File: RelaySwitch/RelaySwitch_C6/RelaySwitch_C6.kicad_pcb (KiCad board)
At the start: 2 copper layers, 67.5 x 52 mm, 39 parts, among them J1 AC_MAINS_IN, J3 LOAD_CH1, J4 LOAD_CH2, J5 SW1_INPUT, J6 SW2_INPUT, K1 G5Q-1-DC5, K2 G5Q-1-DC5, Q1 MMBT8050, Q2 MMBT8050, U1 HLK-2M05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

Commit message: 07/03
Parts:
- removed R10: 1m, Resistor_SMD:R_2512_6332Metric
- added C2: 10u, Capacitor_SMD:C_0402_1005Metric, B.Cu at (190.5, 80.0)
- added C3: 100n, Capacitor_SMD:C_0402_1005Metric, B.Cu at (186.5, 79.5)
- R18: footprint Resistor_SMD:R_Shunt_Vishay_WSK2512_6332Metric_T2.66mm -> XIAO_Series_Footprints:RES_WSK2512R0100FEA
- U2: footprint XIAO_Series_Footprints:XIAO-ESP32-S3-DIP -> XIAO_Series_Footprints:XIAO-ESP32-C6-DIP
- moved C5 31.1 mm to (192.5, 80.0), turned to 0 degrees
- moved R18 12.0 mm to (146.5, 66.5), turned to -90 degrees
- moved C1 0.71 mm to (168.5, 97.5)
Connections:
- C5 pad 1: +3V3 -> +5V
- U5 pad 3: GND -> Net-(U5-V1N)
- U5 pad 4: /L -> GND
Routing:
- net Net-(U5-V1N): track 0.00 -> 32.1 mm, vias 0 -> 1
- net /L: track 57.7 -> 41.3 mm, vias 2 -> 1
- net /L_Sense: track 26.0 -> 35.2 mm
- net GND: track 146.9 -> 139.4 mm, vias 26 -> 19
- net Net-(J5-Pin_1): track 97.5 -> 91.2 mm
- net Net-(D1-A): track 85.4 -> 81.0 mm
- net /RELAY_CH1_IN: track 58.2 -> 55.1 mm
- net /RELAY_CH2_IN: track 53.6 -> 51.2 mm
- net Net-(U5-V1P): track 43.6 -> 45.9 mm
- net +5V: track 123.4 -> 125.4 mm
- net +3V3: track 35.6 -> 37.2 mm
- net /LOAD_CH1: track 29.0 -> 30.3 mm
- net Net-(J6-Pin_1): track 41.7 -> 40.6 mm
- net /LOAD_CH2: track 15.0 -> 14.2 mm

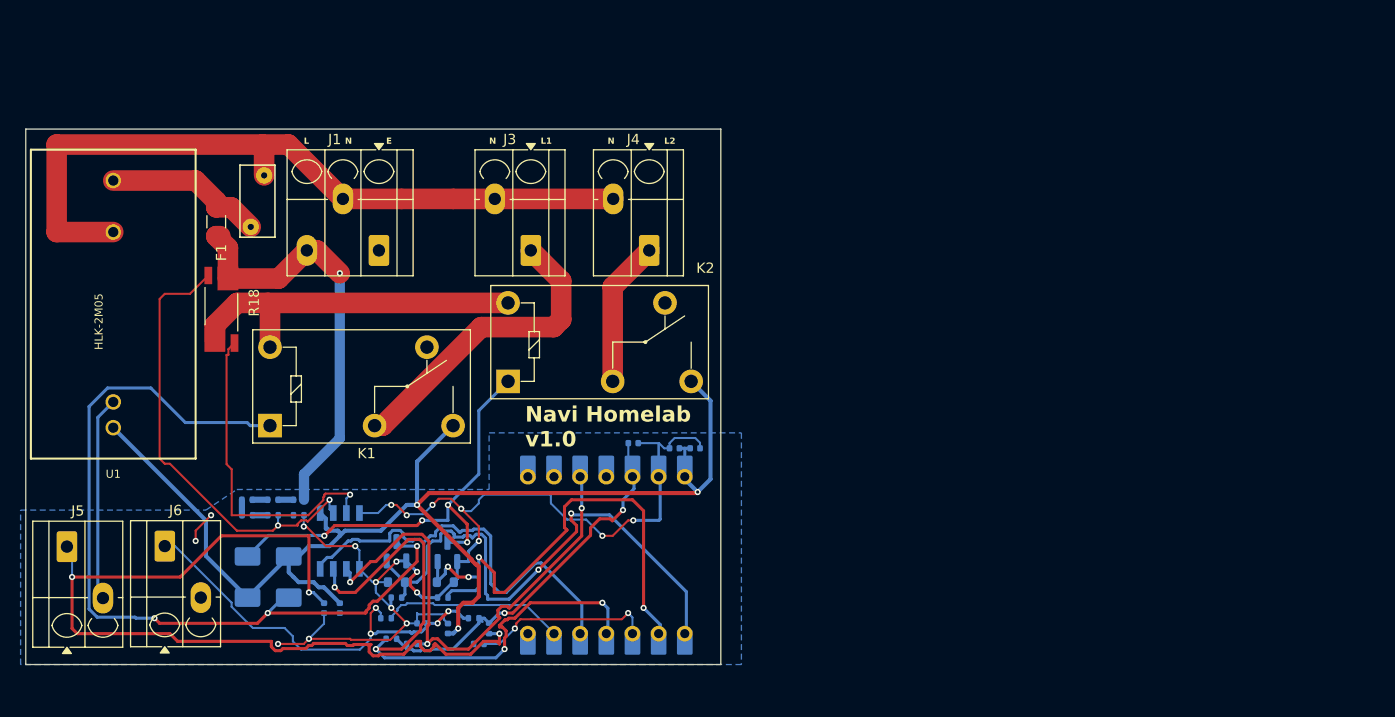
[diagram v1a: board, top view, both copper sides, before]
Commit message: Reduced relay size
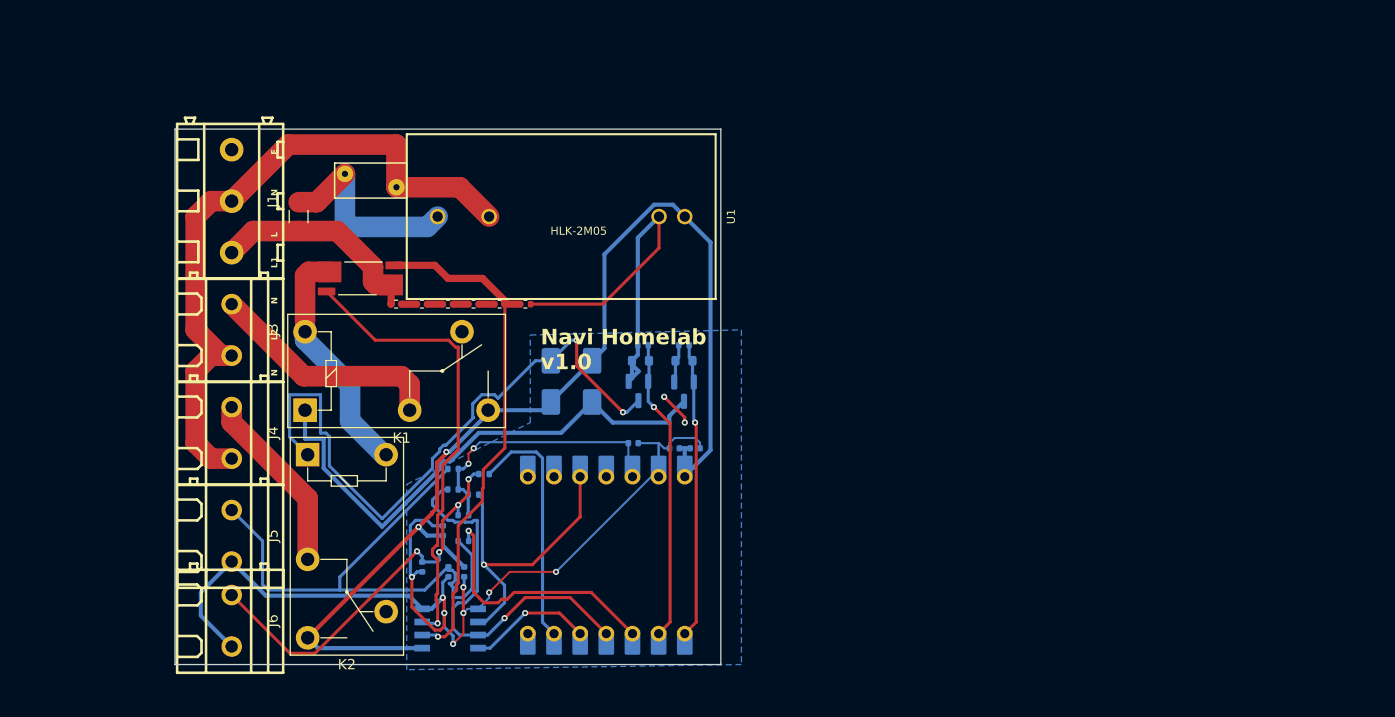
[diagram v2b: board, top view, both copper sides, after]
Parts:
- J1: footprint TerminalBlock_Degson:TerminalBlock_Degson_DG250-3.5-03P_1x03_P3.50mm_45Degree -> seeed esp32:CONN-TH_3P-P5.00_WJ128V-5.0-3P
- J3, J4, J5, J6: footprint TerminalBlock_Degson:TerminalBlock_Degson_DG250-3.5-02P_1x02_P3.50mm_45Degree -> seeed esp32:CONN-TH_2P-P5.00_WJ128V-5.0-2P
- R13, R4, R6, R7, R8, R9: moved to F.Cu
- U5: footprint XIAO_Series_Footprints:SOIC8 -> seeed esp32:SOIC8
- moved U1 44.3 mm to (179.5, 57.5), turned to 0 degrees
- moved J4 44.3 mm to (147.5, 78.5), turned to -90 degrees
- moved D1 37.8 mm to (182.5, 73.5), turned to -90 degrees
- moved R2 37.1 mm to (191.4, 70.0)
- moved R1 35.2 mm to (191.4, 71.5)
- moved D2 32.3 mm to (178.5, 73.5), turned to 90 degrees
- moved Q1 31.9 mm to (191.4, 74.5), turned to -90 degrees
- moved R5 31.3 mm to (187.4, 70.0)
- moved R13 30.1 mm to (173.5, 66.0)
- moved R9 30.1 mm to (176.0, 66.0)
- moved J3 30.1 mm to (147.5, 68.5), turned to -90 degrees
- moved R8 30.0 mm to (171.0, 66.0)
- moved R3 28.7 mm to (187.2, 71.5), turned to 180 degrees
- moved R7 27.2 mm to (168.5, 66.0), turned to 0 degrees
- moved Q2 24.3 mm to (187.0, 74.4), turned to -90 degrees
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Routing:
- net Net-(C7-Pad1): track 91.2 -> 55.3 mm, vias 3 -> 0
- net Net-(D1-A): track 81.0 -> 52.0 mm, vias 3 -> 0
- net /HLW_SEL: track 40.9 -> 12.2 mm, vias 0 -> 1
- net /RELAY_CH1_IN: track 55.1 -> 28.7 mm, vias 2 -> 1
- net /RELAY_CH2_IN: track 51.2 -> 29.4 mm, vias 4 -> 1
- net /HLW_CF1: track 58.5 -> 37.6 mm, vias 4 -> 1
- net /L: track 41.3 -> 21.2 mm, vias 1 -> 0
- net /HLW_CF: track 49.7 -> 30.1 mm, vias 3 -> 1
- net Net-(D2-A): track 43.7 -> 63.1 mm, vias 4 -> 2
- net +5V: track 125.4 -> 110.8 mm, vias 3 -> 2
- net /L_Sense: track 35.2 -> 22.3 mm
- net Net-(U5-V1N): track 32.1 -> 44.9 mm
- net +3V3: track 37.2 -> 26.0 mm
- net Net-(U2-GPIO2_A2_D2): track 17.6 -> 25.1 mm, vias 2 -> 1
- net GND: track 139.4 -> 146.7 mm, vias 19 -> 10
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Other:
- board size 67.5 x 52 mm -> 53 x 52 mm

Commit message: For review
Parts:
- C2: footprint Capacitor_SMD:C_0402_1005Metric -> Capacitor_SMD:C_0805_2012Metric
- F1: value ~ -> T250mA/250V
- moved C2 1.41 mm to (189.5, 79.0)
- moved C3 0.50 mm to (186.0, 79.5)
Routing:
- net GND: track 146.7 -> 150.6 mm
- net +5V: track 110.8 -> 113.9 mm
- net Net-(D1-A): track 52.0 -> 51.5 mm
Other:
- outline, holes or cut-outs redrawn

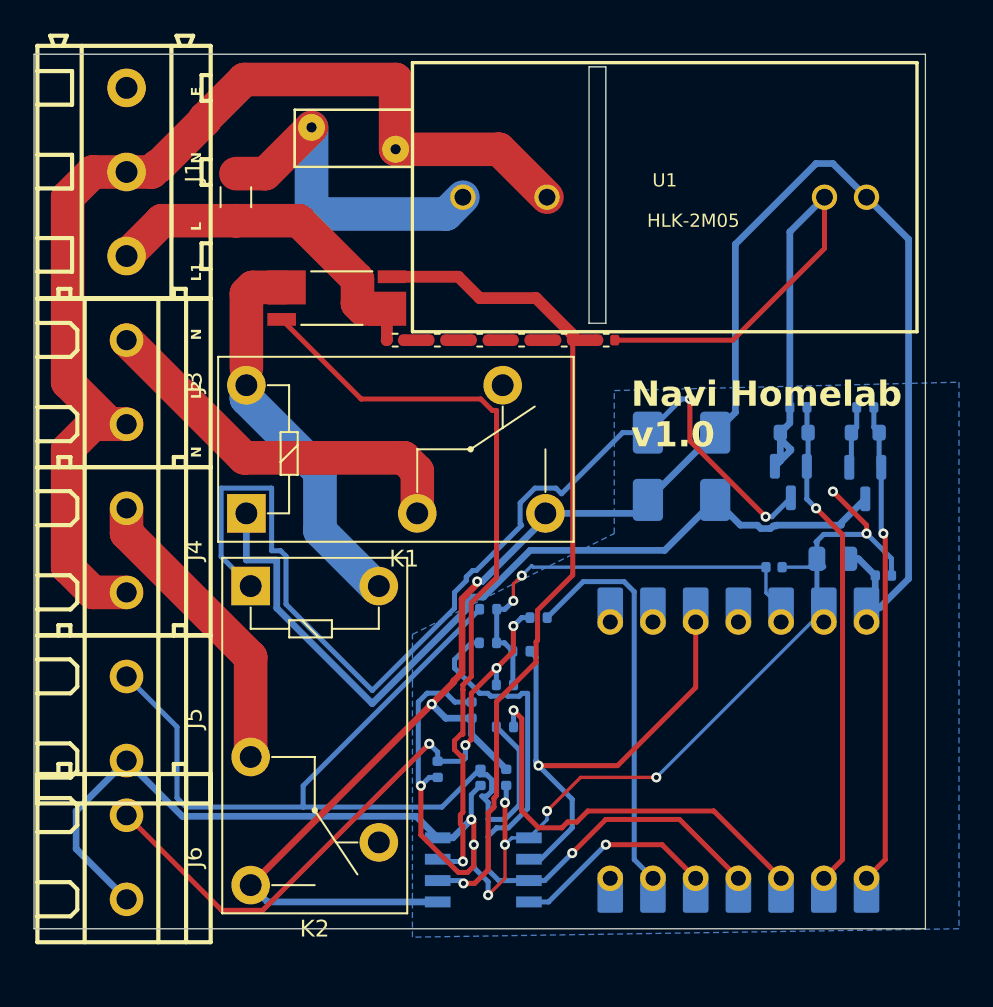
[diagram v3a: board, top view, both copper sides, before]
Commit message: warning fix - 17 left
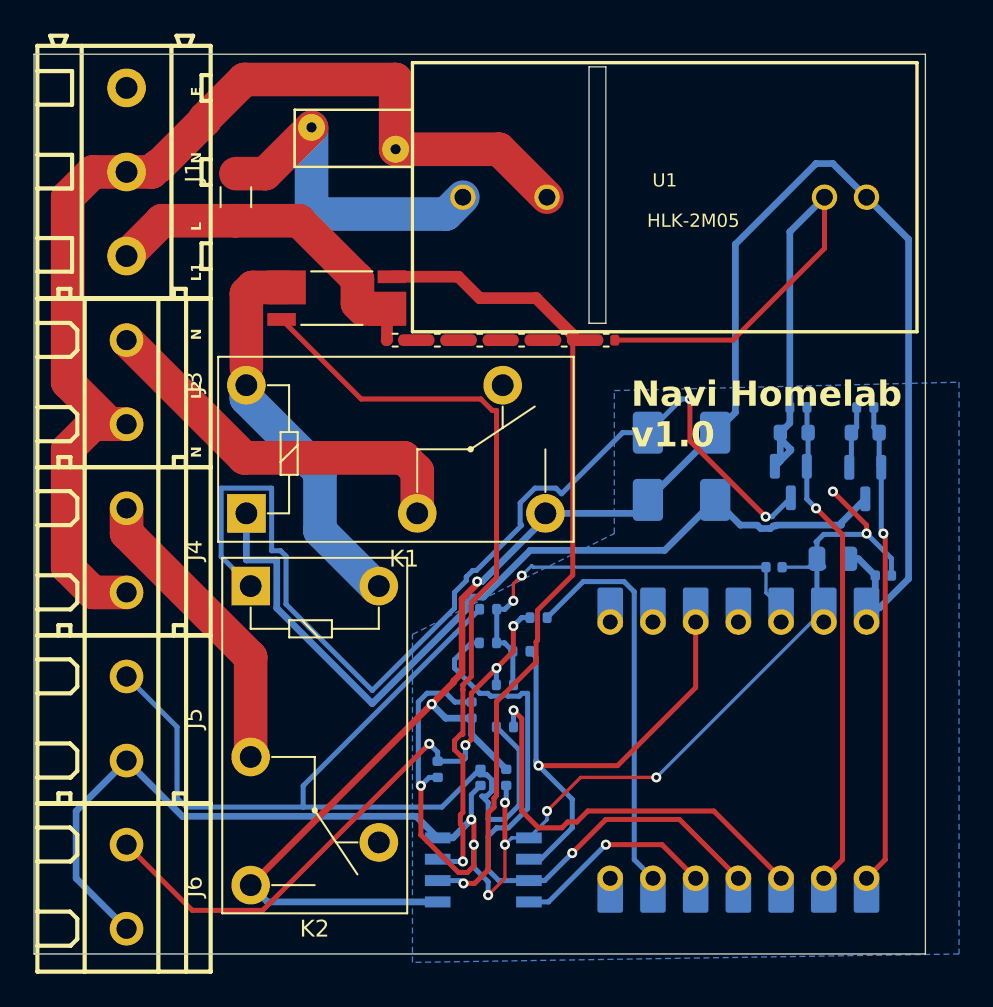
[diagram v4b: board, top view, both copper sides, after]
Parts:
- moved J6 1.75 mm to (147.5, 98.5)
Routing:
- net GND: track 150.6 -> 152.3 mm
- net Net-(C8-Pad1): track 38.7 -> 37.9 mm
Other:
- board size 53 x 52 mm -> 53 x 53.5 mm
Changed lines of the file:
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@@
 			(crossoutdnponfab yes)
 			(subtractmaskfromsilk no)
-			(outputformat 1)
+			(outputformat 5)
 			(mirror no)
-			(drillshape 1)
+			(drillshape 0)
 			(scaleselection 1)
-			(outputdirectory "")
+			(outputdirectory "../Review/")
 		)
 	)
@@
 	(footprint "seeed esp32:CONN-TH_2P-P5.00_WJ128V-5.0-2P"
 		(layer "F.Cu")
-		(at 147.5 96.75 -90)
+		(at 147.5 98.5 -90)
 		(property "Reference" "J6"
 			(at 0 -4 90)
@@
 	)
 	(gr_line
-		(start 142 101)
+		(start 142 102.5)
 		(end 142 49)
 		(stroke
@@
 	(gr_line
 		(start 195 49)
-		(end 195 101)
+		(end 195 102.5)
 		(stroke
 			(width 0.05)
@@
 	)
 	(gr_line
-		(start 195 101)
-		(end 142 101)
+		(start 195 102.5)
+		(end 142 102.5)
 		(stroke
 			(width 0.05)
@@
 	)
 	(segment
-		(start 144.5 94)
-		(end 147.5 91)
+		(start 147.5 91)
+		(end 144.5 94)
 		(width 0.4)
 		(layer "B.Cu")
@@
 	)
 	(segment
-		(start 147.5 99.25)
-		(end 144.5 96.25)
-		(width 0.4)
+		(start 190.915 70)
+		(end 190.915 71.185)
+		(width 0.3)
 		(layer "B.Cu")
 		(net 3)
 	)
 	(segment
-		(start 190.915 70)
-		(end 190.915 71.185)
-		(width 0.3)
+		(start 144.5 98)
+		(end 147.5 101)
+		(width 0.4)
 		(layer "B.Cu")
 		(net 3)
@@
 	)
 	(segment
+		(start 144.5 94)
+		(end 144.5 98)
+		(width 0.4)
+		(layer "B.Cu")
+		(net 3)
+	)
+	(segment
 		(start 186.94 70)
 		(end 186.94 70.935)
@@
 	)
 	(segment
-		(start 144.5 96.25)
-		(end 144.5 94)
-		(width 0.4)
-		(layer "B.Cu")
-		(net 3)
-	)
-	(segment
 		(start 171.424 95.595)
 		(end 170.405 95.595)
@@
 	)
 	(segment
-		(start 153.156 99.906)
-		(end 155.594 99.906)
+		(start 155.594 99.906)
+		(end 151.406 99.906)
 		(width 0.3)
 		(layer "F.Cu")
@@
 	)
 	(segment
-		(start 147.5 94.25)
-		(end 153.156 99.906)
+		(start 151.406 99.906)
+		(end 147.5 96)
 		(width 0.3)
 		(layer "F.Cu")
@@
 	)
 	(segment
-		(start 155.594 99.906)
-		(end 165.5 90)
+		(start 168 89.734948)
+		(end 168 87)
 		(width 0.3)
 		(layer "F.Cu")
@@
 	)
 	(segment
-		(start 168 89.734948)
-		(end 168 87)
+		(start 167.649999 90.084949)
+		(end 168 89.734948)
 		(width 0.3)
 		(layer "F.Cu")
@@
 	)
 	(segment
-		(start 167.649999 90.084949)
-		(end 168 89.734948)
+		(start 165.5 90)
+		(end 155.594 99.906)
 		(width 0.3)
 		(layer "F.Cu")
@@
 		(polygon
 			(pts
-				(xy 176 65.336264) (xy 176 48.836264) (xy 177.5 48.836264) (xy 177.5 65.336264)
+				(xy 176.5 65.336264) (xy 176.5 48.836264) (xy 178 48.836264) (xy 178 65.336264)
 			)
 		)
@@
 		(polygon
 			(pts
-				(xy 164.5 85.5) (xy 164.5 83.5) (xy 176.5 77.5) (xy 176.5 69) (xy 197 68.5) (xy 197 101) (xy 164.5 101.5)
+				(xy 164.5 85.5) (xy 164.5 83.5) (xy 176.5 77.5) (xy 176.5 69) (xy 197 68.5) (xy 197 102.5) (xy 164.5 103)
 				(xy 164.5 86.5)
 			)

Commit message: Fixed relay connections and F1 Fuse
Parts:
- added C10: 33n, Capacitor_SMD:C_0402_1005Metric, F.Cu at (213.6, 78.9)
- added C11: 33n, Capacitor_SMD:C_0402_1005Metric, F.Cu at (213.6, 80.9)
- added C4: 0.1u, Capacitor_SMD:C_0402_1005Metric, F.Cu at (213.6, 75.0)
- added C9: 33n, Capacitor_SMD:C_0402_1005Metric, F.Cu at (213.6, 77.0)
- added R19: 1k, Resistor_SMD:R_0402_1005Metric, F.Cu at (216.5, 75.0)
- added R20: 1k, Resistor_SMD:R_0402_1005Metric, F.Cu at (216.5, 77.0)
- C6: value 100n -> 10u
- F1: footprint Fuse:Fuse_1206_3216Metric -> Fuse:Fuseholder_Clip-5x20mm_Littelfuse_111_Inline_P20.00x5.00mm_D1.05mm_Horizontal
- moved R18 49.9 mm to (209.5, 57.5)
- moved RV1 24.4 mm to (180.0, 41.9)
- moved F1 14.6 mm to (152.0, 43.0), turned to 0 degrees
- moved K1 9.97 mm to (161.8, 69.4), turned to 90 degrees
- moved R6 1.76 mm to (167.7, 66.0)
- moved R13 1.75 mm to (175.3, 66.0)
- moved R4 1.75 mm to (165.2, 66.0)
- moved R7 1.75 mm to (170.3, 66.0)
- moved R8 1.75 mm to (172.7, 66.0)
- moved R9 1.75 mm to (177.8, 66.0)
- moved K2 1.65 mm to (154.2, 82.1)
- moved J1 0.91 mm to (146.6, 56.0)
- moved J3 0.91 mm to (146.6, 68.5)
- moved J4 0.91 mm to (146.6, 78.5)
- moved J5 0.91 mm to (146.6, 88.5)
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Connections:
- F1 pad 2: /MAINS_L -> GND
- K1 pad 1: Net-(D1-A) -> +5V
- K1 pad 3: +5V -> Net-(D1-A)
- K2 pad 1: Net-(D2-A) -> +5V
- K2 pad 3: +5V -> Net-(D2-A)
- Q1 pad 2: /RELAY_CH1_IN -> Net-(Q1-B)
- Q2 pad 2: /RELAY_CH2_IN -> Net-(Q2-B)
- R1 pad 2: GND -> Net-(Q1-B)
- R13 pad 2: Net-(U5-V1P) -> Net-(U5-V2P)
- R18 pad E1: Net-(U5-V1P) -> Net-(R18-PadE1)
- R18 pad E2: Net-(U5-V1N) -> Net-(R18-PadE2)
- R2 pad 2: /RELAY_CH1_IN -> Net-(Q1-B)
- R3 pad 2: GND -> Net-(Q2-B)
- R4 pad 1: /L -> /MAINS_N
- R5 pad 2: /RELAY_CH2_IN -> Net-(Q2-B)
- R9 pad 1: Net-(U5-V1P) -> Net-(U5-V2P)
- RV1 pad 1: /MAINS_L -> GND
- U1 pad 1: /MAINS_L -> GND
- U5 pad 4: GND -> Net-(U5-V2P)
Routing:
- net Net-(U5-V1N): track 44.9 -> 1.56 mm
- net /MAINS_N: track 67.6 -> 34.9 mm
- net Net-(D2-A): track 63.1 -> 38.8 mm
- net /LOAD_CH1: track 23.0 -> 0.00 mm
- net /L_Sense: track 22.3 -> 0.00 mm
- net /L: track 21.2 -> 0.00 mm
- net /MAINS_L: track 20.2 -> 0.00 mm
- net /LOAD_CH2: track 17.8 -> 0.00 mm
- net Net-(D1-A): track 51.5 -> 36.0 mm
- net Net-(U5-V1P): track 51.0 -> 37.0 mm
- net +5V: track 113.9 -> 116.4 mm
- net Net-(U5-V2P): track 0.00 -> 1.48 mm
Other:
- outline, holes or cut-outs redrawn

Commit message: relay after layout design
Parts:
- C10, C11, C4, C9, R19, R20: moved to B.Cu
- F1: value T250mA/250V -> Littelfuse 443.500; footprint Fuse:Fuseholder_Clip-5x20mm_Littelfuse_111_Inline_P20.00x5.00mm_D1.05mm_Horizontal -> easyeda2kicad:0443500DR
- moved R19 46.3 mm to (171.5, 64.0), turned to 90 degrees
- moved C10 44.0 mm to (171.5, 66.0), turned to -90 degrees
- moved R20 43.2 mm to (176.0, 62.0), turned to 180 degrees
- moved C4 42.7 mm to (171.5, 68.0), turned to 90 degrees
- moved C11 42.5 mm to (176.0, 61.0), turned to 180 degrees
- moved R18 40.5 mm to (169.0, 57.0), turned to 0 degrees
- moved C9 39.3 mm to (177.5, 61.5), turned to 90 degrees
- moved R5 33.7 mm to (168.0, 97.5), turned to 180 degrees
- moved U5 31.5 mm to (175.6, 66.7), turned to -90 degrees
- moved R3 30.3 mm to (168.5, 95.3), turned to 90 degrees
- moved D2 28.2 mm to (169.0, 100.0), turned to 0 degrees
- moved Q2 26.6 mm to (171.5, 96.0), turned to 0 degrees
- moved C5 25.7 mm to (176.5, 100.0), turned to 180 degrees
- moved C2 24.2 mm to (179.5, 101.0), turned to 0 degrees
- moved C6 24.0 mm to (170.5, 68.0), turned to 90 degrees
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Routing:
- net GND: track 152.3 -> 38.5 mm, vias 10 -> 0
- net +5V: track 116.4 -> 53.1 mm, vias 2 -> 0
- net Net-(D2-A): track 38.8 -> 0.00 mm, vias 2 -> 0
- net Net-(C8-Pad1): track 37.9 -> 0.00 mm, vias 4 -> 0
- net /HLW_CF1: track 37.6 -> 0.00 mm, vias 1 -> 0
- net Net-(C7-Pad1): track 55.3 -> 20.9 mm
- net /MAINS_N: track 34.9 -> 66.6 mm
- net /L: track 0.00 -> 31.2 mm
- net Net-(U5-V1P): track 37.0 -> 5.82 mm, vias 1 -> 0
- net /HLW_CF: track 30.1 -> 0.00 mm, vias 1 -> 0
- net /RELAY_CH2_IN: track 29.4 -> 0.00 mm, vias 1 -> 0
- net /RELAY_CH1_IN: track 28.7 -> 0.00 mm, vias 1 -> 0
- net +3V3: track 25.7 -> 0.00 mm, vias 2 -> 0
- net Net-(U2-GPIO2_A2_D2): track 25.1 -> 0.00 mm, vias 1 -> 0
- net Net-(U2-GPIO23_D5_SCL): track 23.8 -> 0.00 mm
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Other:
- outline, holes or cut-outs redrawn

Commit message: Complete layout
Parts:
- C1, C9: moved to F.Cu
- moved C11 33.4 mm to (162.5, 91.5), turned to 90 degrees
- moved R20 32.4 mm to (161.5, 91.0), turned to 90 degrees
- moved U5 30.6 mm to (157.0, 91.0), turned to 180 degrees
- moved R12 27.6 mm to (152.5, 93.0), turned to -90 degrees
- moved D1 27.4 mm to (155.5, 100.5)
- moved R11 26.8 mm to (152.5, 91.0), turned to 90 degrees
- moved R19 26.1 mm to (163.8, 89.0), turned to 0 degrees
- moved R2 25.3 mm to (161.5, 97.0)
- moved C10 24.9 mm to (161.8, 89.0), turned to 180 degrees
- moved Q1 24.9 mm to (158.9, 96.5)
- moved R1 24.7 mm to (163.5, 97.0)
- moved K2 24.2 mm to (165.0, 61.2)
- moved C4 21.5 mm to (161.5, 87.0)
- moved C6 20.6 mm to (162.5, 87.0)
- moved R17 16.5 mm to (172.5, 81.5)
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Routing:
- net GND: track 38.5 -> 116.9 mm, vias 0 -> 7
- net +5V: track 53.1 -> 110.4 mm, vias 0 -> 4
- net Net-(R18-PadE2): track 0.00 -> 53.3 mm, vias 0 -> 1
- net Net-(R18-PadE1): track 0.00 -> 46.3 mm, vias 0 -> 1
- net +3V3: track 0.00 -> 45.1 mm, vias 0 -> 3
- net /HLW_CF: track 0.00 -> 42.8 mm, vias 0 -> 2
- net Net-(U5-V2P): track 0.00 -> 42.1 mm, vias 0 -> 3
- net /HLW_CF1: track 0.00 -> 38.4 mm
- net Net-(C8-Pad1): track 0.00 -> 37.8 mm
- net /HLW_SEL: track 0.00 -> 36.9 mm
- net /RELAY_CH2_IN: track 0.00 -> 30.0 mm, vias 0 -> 1
- net /L_Sense: track 10.7 -> 39.0 mm
- net Net-(D2-A): track 0.00 -> 28.2 mm, vias 0 -> 1
- net Net-(D1-A): track 23.3 -> 51.3 mm, vias 0 -> 2
- net /RELAY_CH1_IN: track 0.00 -> 23.0 mm, vias 0 -> 1
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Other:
- outline, holes or cut-outs redrawn
